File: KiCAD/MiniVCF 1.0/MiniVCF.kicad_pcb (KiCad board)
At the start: 2 copper layers, 94 x 128.5 mm, 84 parts, among them J1 JST_BUS, J10 CV2, J11 CTRL_PANEL_CONN2, J12 MAIN_BOARD_CONN2, J2 IDC_BUS, J3 AudioIn, J4 CV1, J5 AudioOut, J6 CONN_PWR1, J7 CONN_PWR2, J8 MAIN_BOARD_CONN, J9 CTRL_PANEL_CONN, U1 TL074, U2 TL074

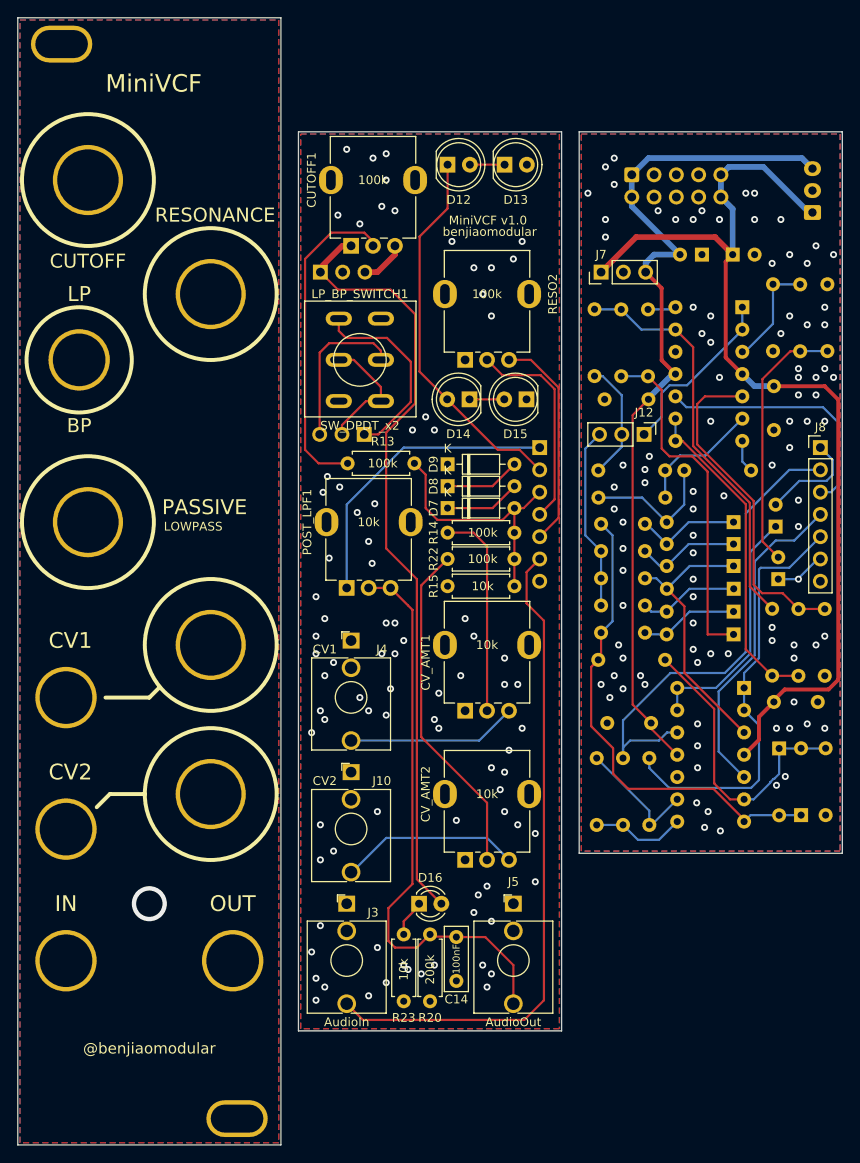
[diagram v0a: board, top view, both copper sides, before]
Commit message: Fixed toggle switch connections
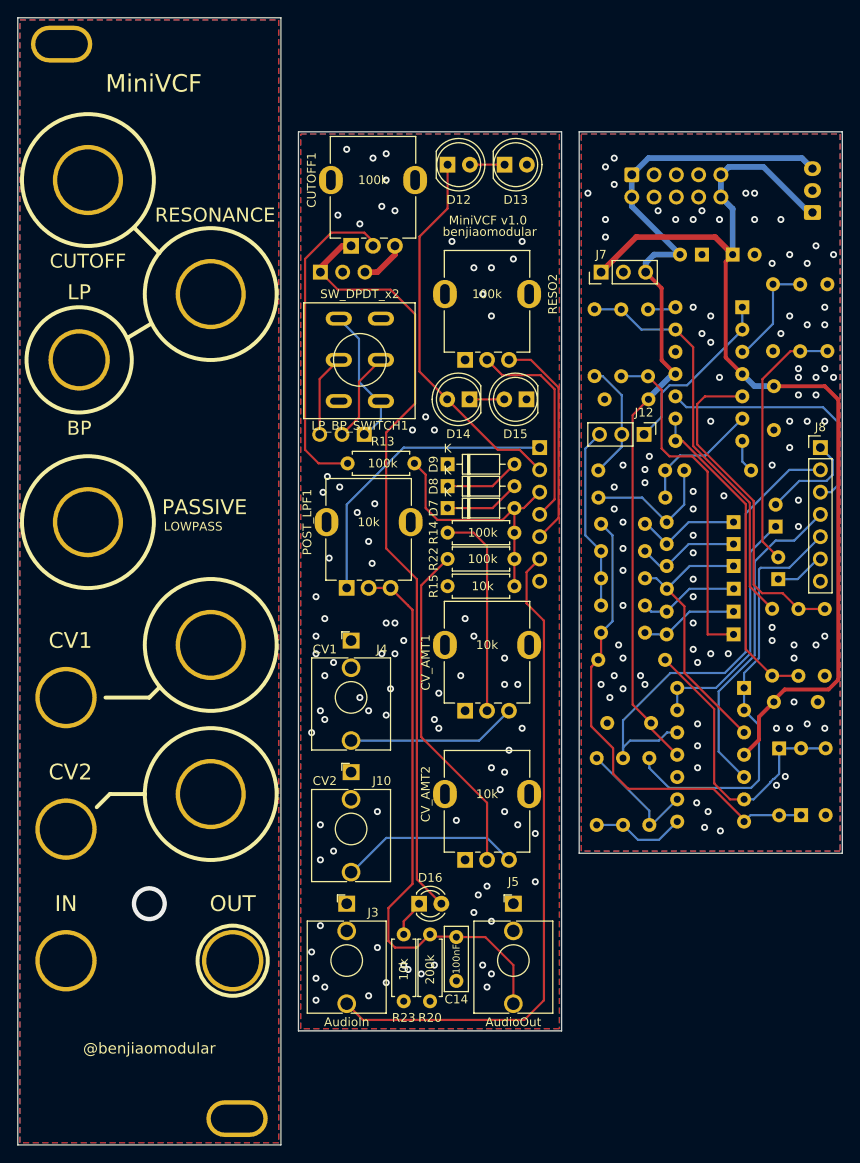
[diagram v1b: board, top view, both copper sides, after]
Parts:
- turned LP_BP_SWITCH1 to 180 degrees
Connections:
- LP_BP_SWITCH1 pad 6: A_7 -> A_8
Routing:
- net A_9: track 18.1 -> 9.40 mm
- net A_8: track 22.5 -> 16.3 mm
- net A_7: track 14.3 -> 10.3 mm
- net B_AUDIO_IN: vias 1 -> 0

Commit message: Added fab files for v1.0
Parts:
- moved C1 0.63 mm to (126.5, 103.4)
- moved CUTOFF1 0.50 mm to (77.5, 66.0)
- moved CV_AMT1 0.50 mm to (91.5, 119.0)
- moved CV_AMT2 0.50 mm to (91.5, 136.0)
- moved J10 0.50 mm to (77.5, 126.0)
- moved J4 0.50 mm to (77.5, 111.0)
- moved C7 0.41 mm to (126.5, 97.6)
- moved REF** 0.10 mm to (45.5, 125.9)
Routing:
- net A_8: track 16.3 -> 20.6 mm
- net Net-(CV_AMT2-Pad3): track 20.7 -> 22.4 mm
- net Net-(CV_AMT1-Pad3): track 19.4 -> 20.9 mm
- net A_AUDIO_IN: track 75.9 -> 76.9 mm
- net B_6: track 37.2 -> 38.0 mm
- net Net-(CUTOFF1-Pad2): track 37.1 -> 36.4 mm, vias 0 -> 1
- net Net-(C1-Pad2): track 29.8 -> 29.1 mm
- net POS12V_1: track 89.0 -> 88.5 mm
- net GND1: vias 86 -> 94
- net (no net): vias 5 -> 6

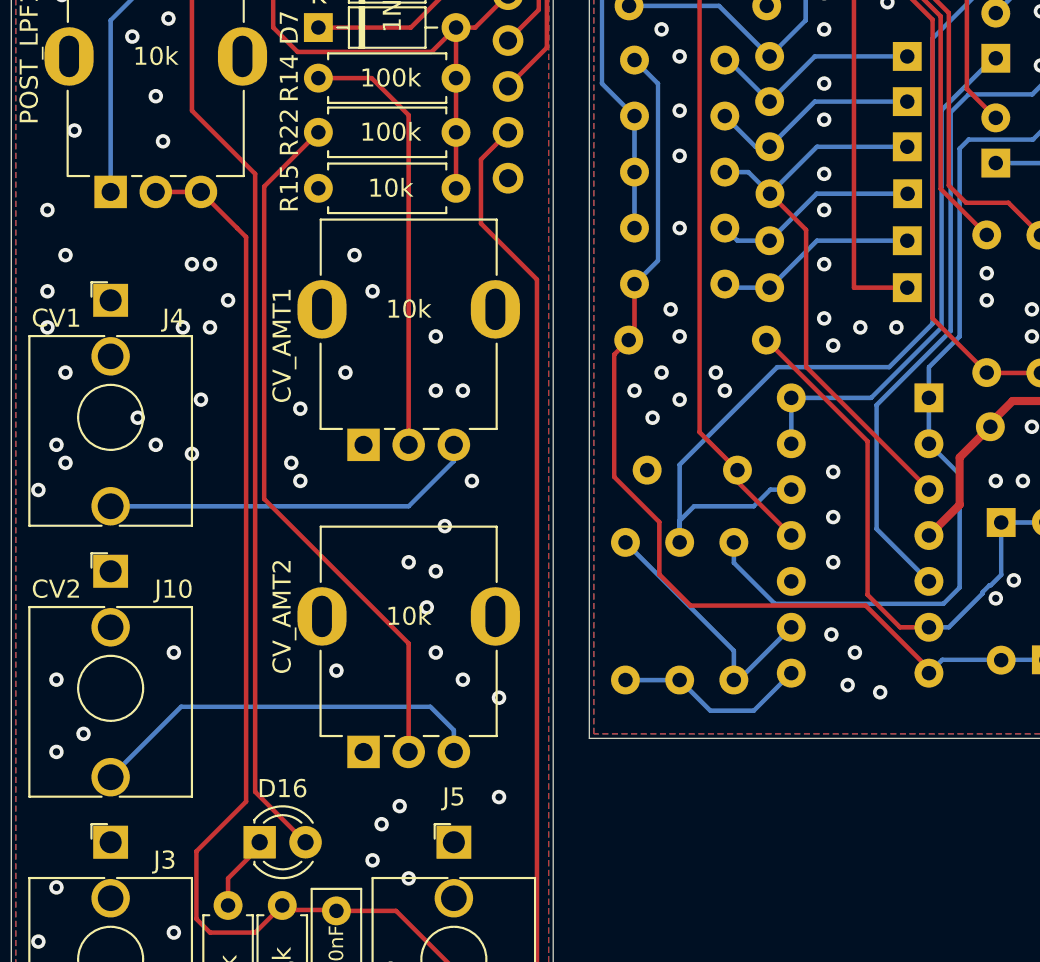
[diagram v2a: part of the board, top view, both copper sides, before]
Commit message: Added a lock hole on control and main board
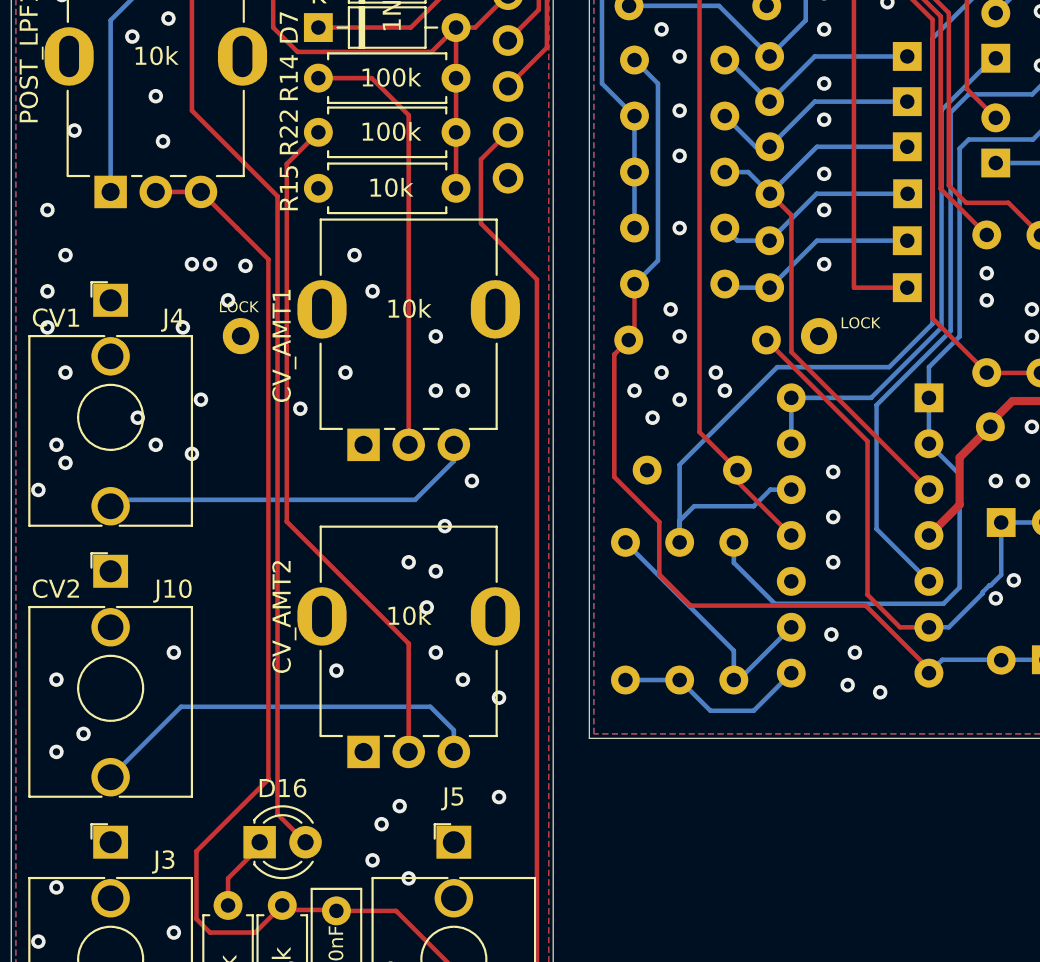
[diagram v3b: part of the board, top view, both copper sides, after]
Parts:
- added REF**: Wire_1mm, benjiaomodular:Wire_1mm, F.Cu at (84.7, 113.0)
- added REF**: Wire_1mm, benjiaomodular:Wire_1mm, F.Cu at (116.7, 113.0)
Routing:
- net Net-(CV_AMT2-Pad2): track 38.9 -> 37.8 mm
- net Net-(C14-Pad2): track 66.0 -> 67.0 mm
- net GND2: vias 91 -> 87
- net GND1: vias 94 -> 92
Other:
- board text added: "LOCK"
